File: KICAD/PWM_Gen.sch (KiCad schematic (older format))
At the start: 13 parts, among them U1 AD8030, U13 AD8030

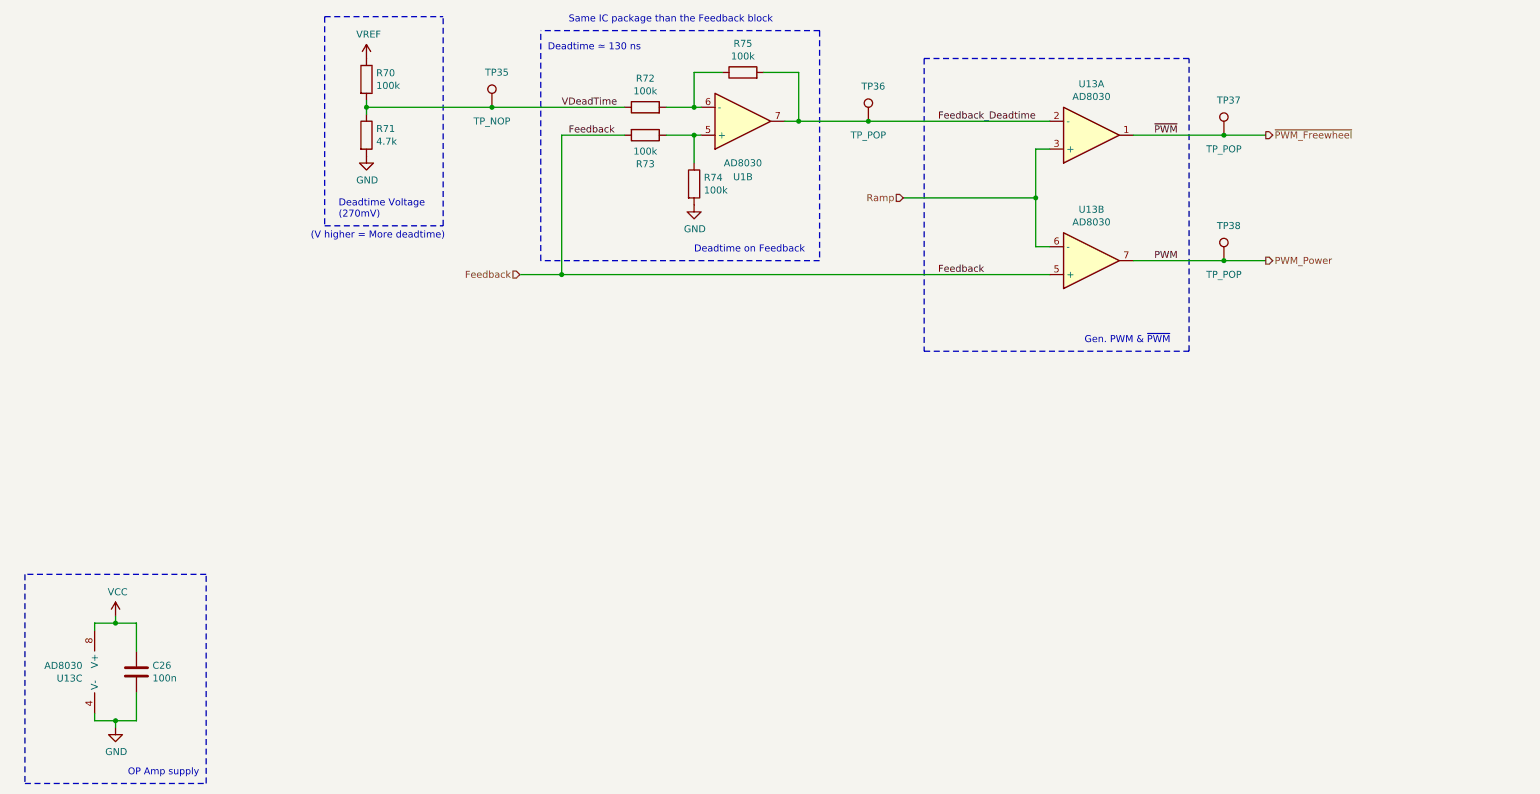
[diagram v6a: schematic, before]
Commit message: modified deadtime + added config pads on the bottom for charge pump config
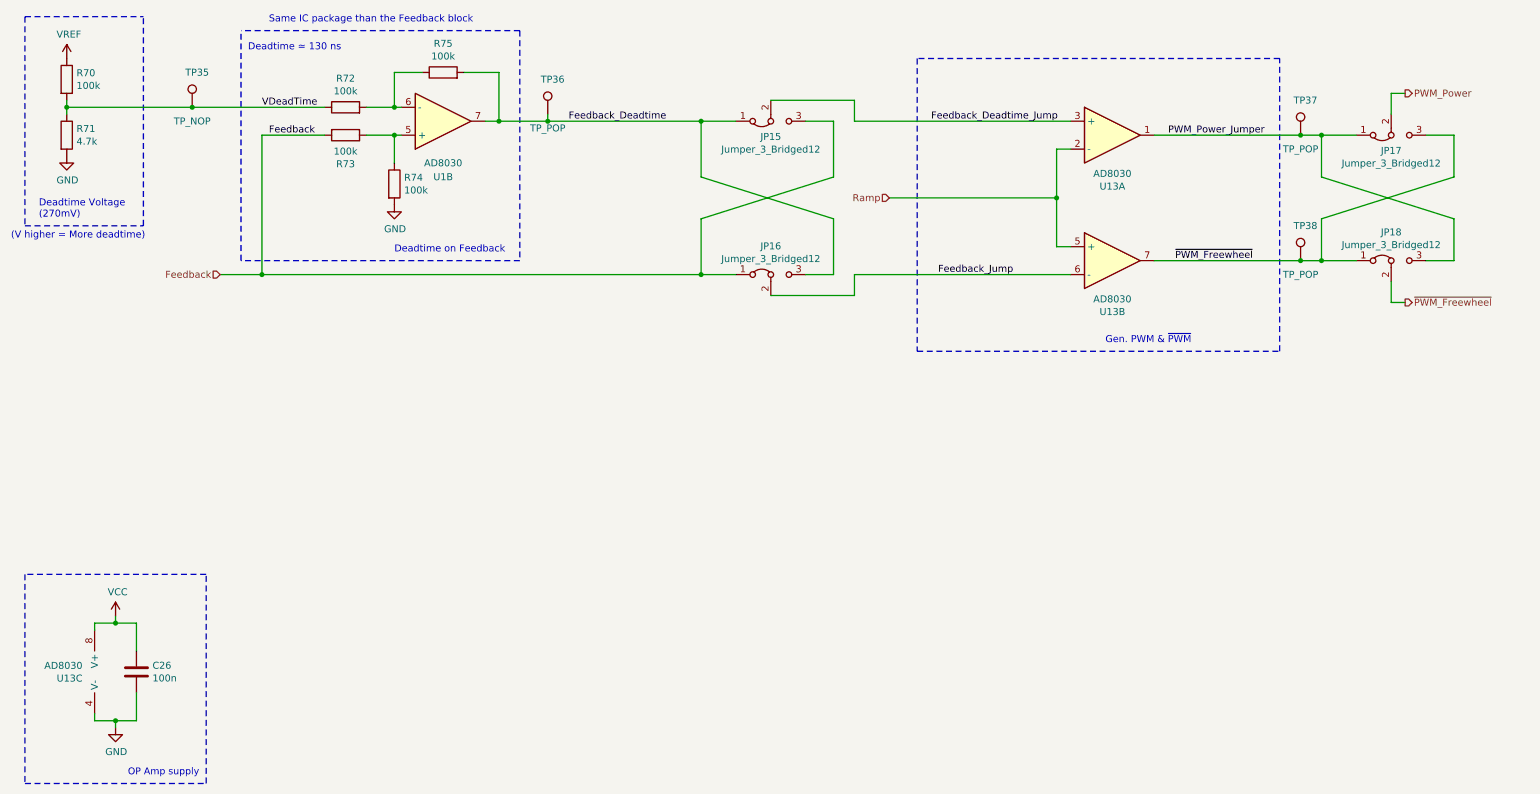
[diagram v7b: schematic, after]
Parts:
- added JP15, JP16, JP17, JP18: Jumper_3_Bridged12, Jumper:SolderJumper-3_P1.3mm_Bridged12_Pad1.0x1.5mm, symbol Jumper:Jumper_3_Bridged12
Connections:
- net Feedback: now also JP15.3 (B), JP16.1 (A); no longer U13.5 (+)
- net Feedback_Deadtime: now also JP15.1 (A), JP16.3 (B); no longer U13.2 (-)
- net PWM_Power: now also JP17.2 (C); no longer TP38.1, U13.7
- net Ramp: now also U13.2 (-), U13.5 (+); no longer U13.3 (+), U13.6 (-)
- net ~PWM_Freewheel: now also TP38.1, U13.7, JP17.3 (B), JP18.1 (A), JP18.2 (C); no longer TP37.1, U13.1
- new net Feedback_Deadtime_Jump: JP15.2 (C), U13.3 (+)
- new net Feedback_Jump: JP16.2 (C), U13.6 (-)
- new net PWM_Power_Jumper: JP17.1 (A), JP18.3 (B), TP37.1, U13.1
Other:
- moved on the sheet: R70, R71, R72, R73, R74, R75, TP35, TP36, TP37, TP38, U13A, U13B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

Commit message: lil cleanup on the main schematic sheet
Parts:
- C26: symbol Device:C -> sesame-fonctionnel-rescue:C-Device
- JP15, JP16, JP17, JP18: symbol Jumper:Jumper_3_Bridged12 -> sesame-fonctionnel-rescue:Jumper_3_Bridged12-Jumper
- R70, R71, R72, R73, R74, R75: symbol Device:R -> sesame-fonctionnel-rescue:R-Device
- TP35, TP36, TP37, TP38: symbol Connector:TestPoint -> sesame-fonctionnel-rescue:TestPoint-Connector
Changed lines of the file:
@@
 Feedback
 $Comp
-L Device:R R?
+L sesame-fonctionnel-rescue:R-Device R?
 U 1 1 613D641B
 P 2850 3050
@@
 $EndComp
 $Comp
-L Device:R R?
+L sesame-fonctionnel-rescue:R-Device R?
 U 1 1 613D6415
 P 2850 2850
@@
 	3950 2950 3850 2950
 $Comp
-L power:GND #PWR?
+L sesame-fonctionnel-rescue:GND-power #PWR?
 U 1 1 613D6432
 P 3200 3550
@@
 	3200 3250 3200 3050
 $Comp
-L Device:R R?
+L sesame-fonctionnel-rescue:R-Device R?
 U 1 1 613D6429
 P 3200 3400
@@
 	3250 2850 3200 2850
 $Comp
-L Device:R R?
+L sesame-fonctionnel-rescue:R-Device R?
 U 1 1 613D9855
 P 850 3050
@@
 $EndComp
 $Comp
-L power:GND #PWR?
+L sesame-fonctionnel-rescue:GND-power #PWR?
 U 1 1 613D9F4F
 P 850 3200
@@
 $EndComp
 $Comp
-L Device:R R?
+L sesame-fonctionnel-rescue:R-Device R?
 U 1 1 613D8CB8
 P 850 2650
@@
 $EndComp
 $Comp
-L Connector:TestPoint TP35
+L sesame-fonctionnel-rescue:TestPoint-Connector TP35
 U 1 1 612937F6
 P 1750 2850
@@
 	850  2850 1750 2850
 $Comp
-L Connector:TestPoint TP36
+L sesame-fonctionnel-rescue:TestPoint-Connector TP36
 U 1 1 61299A59
 P 4300 2900
@@
 $EndComp
 $Comp
-L Connector:TestPoint TP38
+L sesame-fonctionnel-rescue:TestPoint-Connector TP38
 U 1 1 612A9FCA
 P 9700 3950
@@
 OP Amp supply
 $Comp
-L Device:C C26
+L sesame-fonctionnel-rescue:C-Device C26
 U 1 1 612CB355
 P 1350 6900
@@
 	1050 7250 1050 7200
 $Comp
-L power:GND #PWR087
+L sesame-fonctionnel-rescue:GND-power #PWR087
 U 1 1 612CB360
 P 1200 7300
@@
 	1200 7250 1350 7250
 $Comp
-L power:VCC #PWR086
+L sesame-fonctionnel-rescue:VCC-power #PWR086
 U 1 1 612CB36D
 P 1200 6500
@@
 Deadtime ≃ 130 ns
 $Comp
-L Device:R R?
+L sesame-fonctionnel-rescue:R-Device R?
 U 1 1 613D640F
 P 3550 2600
@@
 $EndComp
 $Comp
-L Jumper:Jumper_3_Bridged12 JP17
+L sesame-fonctionnel-rescue:Jumper_3_Bridged12-Jumper JP17
 U 1 1 614ED0FD
 P 10350 3050
@@
 	10450 2750 10350 2750
 $Comp
-L Jumper:Jumper_3_Bridged12 JP18
+L sesame-fonctionnel-rescue:Jumper_3_Bridged12-Jumper JP18
 U 1 1 614F10A9
 P 10350 3950
@@
 	5650 4050 5400 4050
 $Comp
-L Jumper:Jumper_3_Bridged12 JP15
+L sesame-fonctionnel-rescue:Jumper_3_Bridged12-Jumper JP15
 U 1 1 61517849
 P 5900 2950
@@
 	5400 2950 5650 2950
 $Comp
-L Jumper:Jumper_3_Bridged12 JP16
+L sesame-fonctionnel-rescue:Jumper_3_Bridged12-Jumper JP16
 U 1 1 61517850
 P 5900 4050
@@
 	6950 4600 9550 4600
 $Comp
-L Connector:TestPoint TP37
+L sesame-fonctionnel-rescue:TestPoint-Connector TP37
 U 1 1 612A923F
 P 9700 3050
